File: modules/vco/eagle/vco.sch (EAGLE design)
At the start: 38 parts, among them IC1 TL074P, IC2 TL072P, Q1 J107, T1 2N3904, T2 2N3904

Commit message: Finish up 1x VCO schematic in eagle
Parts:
- added C10: 10p, rcl:C-EU025-024X044
- added C11, C12: 100p, rcl:C-EU025-024X044
- added C13, C14, C15, C16, C17, C18, C19, C20: 10u, rcl:CPOL-EUE1.8-4
- added C8: 2.2n, rcl:C-EU025-024X044
- added C9: 100n, rcl:C-EU025-024X044
- added D3, D4: 1N4148, diode:1N4148DO35-7
- added IC3, IC4: TL072P, linear:TL072P
- added R25: 2K, pot:TRIM_EU-B64Y
- added R26, R27, R28, R29, R41, R42, R54: 10K, resistor:R-EU_0204/7
- added R30, R31, R56: 100K, resistor:R-EU_0204/7
- added R32, R33: 1M, resistor:R-EU_0204/7
- added R34, R38: 15K, resistor:R-EU_0204/7
- added R35: 33K, resistor:R-EU_0204/7
- added R36, R58: 20K, resistor:R-EU_0204/7
- added R37, R50, R62: 1K, resistor:R-EU_0204/7
- added R39: 10K, pot:TRIM_EU-CA6V
- added R40: 390R, resistor:R-EU_0204/7
- added R43, R51, R52, R61: 22K, resistor:R-EU_0204/7
- added R44, R49: 4K7, resistor:R-EU_0204/7
- added R45, R46: 2K2, resistor:R-EU_0204/7
- added R47: 100K, pot:TRIM_EU-CA6V
- added R48: 50K, pot:TRIM_EU-CA6V
- added R53: 56K, resistor:R-EU_0204/7
- added R55: 150K, resistor:R-EU_0204/7
- added R57: 10M, resistor:R-EU_0204/7
- added R59: 8K2, resistor:R-EU_0204/7
- added R60: 3K3, resistor:R-EU_0204/7
- added T3, T4: 2N3904, transistor:2N3904
- added X1, X10, X2, X5, X6, X7, X8, X9: 22-23-2031, con-molex:22-23-2031
- added X11, X13, X3: (no value), con-wago-500:W237-103
- added X12, X4: (no value), con-wago-500:W237-102
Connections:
- new net N$19: R23.1, R25.E
- new net N$21: R24.2, R25.A
- new net N$24: IC3A.-IN, R34.2, R35.1
- new net N$25: IC2A.-IN, R25.S
- new net N$26: IC2B.+IN, R26.2, R27.1
- new net N$27: R28.1, X3-2.KL
- new net N$28: R5.1, X3-1.KL
- new net N$29: R29.1, X3-3.KL
- new net N$30: R29.2, X7-3.S
- new net N$31: R28.2, X5-3.S
- new net N$32: X5-2.S, X6-2.S
- new net N$33: X7-2.S, X8-2.S
- new net N$34: R30.1, X6-3.S
- new net N$35: R31.1, X8-3.S
- new net N$36: R32.1, X6-1.S
- new net N$37: R33.1, X8-1.S
- new net N$38: R52.1, X9-1.S
- new net N$39: C8.1, D3.C, D4.C, R34.1, R36.2
- new net N$40: R51.2, X9-3.S
- new net N$41: R54.1, X9-2.S
- new net N$42: D3.A, IC2B.OUT, R27.2, X12-1.KL
- new net N$43: R38.1, R39.A
- new net N$44: C9.1, IC3A.+IN, R39.S
- new net N$45: R40.2, R48.A, T3.E
- new net N$46: R40.1, R48.E, T4.E
- new net N$47: IC3B.-IN, R41.1, R44.2, T3.C
- new net N$48: IC3B.+IN, R42.1, R43.2, T4.C
- new net N$49: R53.1, X10-2.S, X10-3.S, X4-2.KL
- new net N$50: C10.2, IC4A.OUT, R57.2, R58.1
- new net N$51: IC3B.OUT, R44.1, R50.2
- new net N$52: R45.2, T4.B
- new net N$53: R46.2, R47.E, T3.B
- new net N$54: C11.1, C12.2, IC4B.-IN, R58.2, R59.1
- new net N$55: C11.2, IC4B.OUT, R59.2, R60.1
- new net N$56: R48.S, R49.2
- new net N$EXP-CV1: C1.2, IC1A.-IN, R1.2, R2.2, R3.1, R30.2, R31.2, R5.2
- new net N$LIN-CV1: C2.2, IC1B.-IN, R11.1, R32.2, R33.2, T1.C
- new net N$PULSE-OUT1: R60.2, R61.2, X11-1.KL
- new net N$PW-CV1: IC4A.+IN, R53.2, R54.2, R55.2
- new net N$SAW-OUT1: D4.A, IC2A.OUT, R21.2, R22.2, R26.1, R56.1, X12-2.KL
- new net N$SAW-OUT2: R62.2
- new net N$SINE-OUT1: R50.1, X11-2.KL
- new net N$TRI-OUT1: IC3A.OUT, R35.2, R37.2, R47.A, R47.S, X11-3.KL
- net GND: now also C12.1, C13.-, C14.+, C15.-, C16.+, C17.-, C18.+, C19.-, C20.+, C9.2, IC2B.-IN, IC4B.+IN, R22.1, R24.1, R37.1, R39.E, R43.1, R45.1, R46.1, R55.1, R61.1, R62.1, X10-1.S, X13-2.KL, X5-1.S, X7-1.S
- net N$1: now also R1.1, X1-2.S; no longer C1.2, IC1A.-IN, R1.2, R2.2, R3.1, R5.2
- net N$12: now also C10.1, IC4A.-IN, R56.2, R57.1; no longer C2.2, IC1B.-IN, R11.1, T1.C
- net N$14: now also R20.1
- net N$17: now also X4-1.KL
- net N$23: now also R2.1, X2-2.S; no longer IC2A.OUT, R21.2
- net VCC: now also C13.+, C15.+, C17.+, C19.+, IC1P.V+, IC2P.V+, IC3P.V+, IC4P.V+, R23.2, R38.2, R41.2, R42.2, R51.1, X1-3.S, X13-1.KL, X2-3.S
- net VEE: now also C14.-, C16.-, C18.-, C20.-, C8.2, IC1P.V-, IC2P.V-, IC3P.V-, IC4P.V-, R36.1, R49.1, R52.2, X1-1.S, X13-3.KL, X2-1.S
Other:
- note added: "100K LIN POT"
- note added: "FM1"
- note added: "FM1 DEPTH 100K LIN POT"
- note added: "FM1 EXP/LIN SPDT"
- note added: "FM2"
- note added: "FM2 DEPTH 100K LIN POT"
- note added: "FM2 EXP/LIN SPDT"
- note added: "POWER"
- note added: "PULSE OUT"
- note added: "PULSE WIDTH 100K LIN POT"
- note added: "PW"
- note added: "PWM DEPTH 100K LIN POT"
- note added: "RAMP OUT"
- note added: "SAW OUT"
- note added: "SINE OUT"
- note added: "TRIANGLE OUT"
- note removed: "TODO: - FM inputs - FM depth pot connectors - FM mode (EXP/LIN) switch connectors"
- moved on the sheet: C3, C4, C6, C7, D2, IC1C, IC1D, IC2A, IC2B, Q1, R12, R13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

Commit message: Add 2-layer VCO Eagle board design
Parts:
- added C21: 100n, rcl:C-EU025-024X044
- added IC5: TL072P, linear:TL072P
- added R63: 47R, resistor:R-EU_0204/7
- added R64: 1K, resistor:R-EU_0204/7
- added R65: 1M, resistor:R-EU_0204/7
- added X14, X15: 22-23-2031, con-molex:22-23-2031
- R4: value 3K3 -> 3K9
- R7: value 470R -> 390R
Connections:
- removed net N$42: D3.A, IC2B.OUT, R27.2, X12-1.KL
- new net N$57: R63.2, R8.E
- new net N$58: R64.1, X14-2.S, X14-3.S
- new net N$59: C21.1, IC5A.+IN, R64.2
- new net N$60: IC5A.-IN, IC5A.OUT, R6.1
- new net N$61: R65.1, X15-2.S
- net GND: now also C21.2, IC5B.+IN, IC5B.-IN
- net N$13: now also Q1.S; no longer Q1.D
- net N$14: now also Q1.D; no longer Q1.S
- net N$2: now also X14-1.S; no longer R6.1
- net N$4: now also R63.1; no longer R8.E
- net N$LIN-CV1: now also R65.2
- net N$SAW-OUT2: now also D3.A, IC2B.OUT, R27.2, X12-1.KL
- net VCC: now also IC5P.V+, X15-3.S
- net VEE: now also IC5P.V-, X15-1.S
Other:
- note added: "LIN DETUNE 100K LIN POT"
- note added: "PORTAMENTO 1M LIN POT"
- moved on the sheet: C10, C11, C12, C13, C14, C15, C16, C17, C18, C19, C20, C5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

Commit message: VCO PCB fixes
- Fixes a couple of design flaws: two opamps hade the inputs the wrong way
  around, the sine output net intersected with a pin connected to ground
- Moves the connector legend to the tName layer so they show up in fab.
- Adds legends to the trimpots
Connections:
- net GND: now also IC2B.+IN; no longer IC2B.-IN
- net N$22: now also IC2A.-IN; no longer IC2A.+IN
- net N$25: now also IC2A.+IN; no longer IC2A.-IN
- net N$26: now also IC2B.-IN; no longer IC2B.+IN
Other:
- moved on the sheet: IC2A, IC2B
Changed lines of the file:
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@@
 <instance part="SUPPLY11" gate="G$1" x="236.22" y="5.08" rot="R180"/>
 <instance part="R19" gate="G$1" x="165.1" y="-12.7" rot="R270"/>
-<instance part="IC2" gate="A" x="289.56" y="50.8"/>
-<instance part="IC2" gate="B" x="289.56" y="5.08"/>
+<instance part="IC2" gate="A" x="289.56" y="50.8" rot="MR180"/>
+<instance part="IC2" gate="B" x="289.56" y="5.08" rot="MR180"/>
 <instance part="R20" gate="G$1" x="271.78" y="53.34"/>
 <instance part="R21" gate="G$1" x="289.56" y="60.96"/>
@@
 </segment>
 <segment>
-<pinref part="IC2" gate="B" pin="-IN"/>
 <pinref part="SUPPLY15" gate="GND" pin="GND"/>
+<wire x1="279.4" y1="2.54" x2="279.4" y2="0" width="0.1524" layer="91"/>
+<pinref part="IC2" gate="B" pin="+IN"/>
 <wire x1="281.94" y1="2.54" x2="279.4" y2="2.54" width="0.1524" layer="91"/>
-<wire x1="279.4" y1="2.54" x2="279.4" y2="0" width="0.1524" layer="91"/>
 </segment>
 <segment>
@@
 <segment>
 <pinref part="R20" gate="G$1" pin="2"/>
-<pinref part="IC2" gate="A" pin="+IN"/>
 <wire x1="276.86" y1="53.34" x2="279.4" y2="53.34" width="0.1524" layer="91"/>
-<wire x1="281.94" y1="53.34" x2="279.4" y2="53.34" width="0.1524" layer="91"/>
 <wire x1="279.4" y1="53.34" x2="279.4" y2="60.96" width="0.1524" layer="91"/>
 <pinref part="R21" gate="G$1" pin="1"/>
 <wire x1="279.4" y1="60.96" x2="284.48" y2="60.96" width="0.1524" layer="91"/>
+<pinref part="IC2" gate="A" pin="-IN"/>
+<wire x1="279.4" y1="53.34" x2="281.94" y2="53.34" width="0.1524" layer="91"/>
 <junction x="279.4" y="53.34"/>
 </segment>
@@
 <pinref part="R25" gate="1" pin="S"/>
 <wire x1="269.24" y1="40.64" x2="269.24" y2="48.26" width="0.1524" layer="91"/>
-<pinref part="IC2" gate="A" pin="-IN"/>
-<wire x1="269.24" y1="48.26" x2="281.94" y2="48.26" width="0.1524" layer="91"/>
+<pinref part="IC2" gate="A" pin="+IN"/>
+<wire x1="281.94" y1="48.26" x2="269.24" y2="48.26" width="0.1524" layer="91"/>
 </segment>
 </net>
@@
 <segment>
 <pinref part="R26" gate="G$1" pin="2"/>
-<pinref part="IC2" gate="B" pin="+IN"/>
 <wire x1="276.86" y1="7.62" x2="279.4" y2="7.62" width="0.1524" layer="91"/>
 <pinref part="R27" gate="G$1" pin="1"/>
-<wire x1="279.4" y1="7.62" x2="281.94" y2="7.62" width="0.1524" layer="91"/>
 <wire x1="284.48" y1="15.24" x2="279.4" y2="15.24" width="0.1524" layer="91"/>
 <wire x1="279.4" y1="15.24" x2="279.4" y2="7.62" width="0.1524" layer="91"/>
+<pinref part="IC2" gate="B" pin="-IN"/>
+<wire x1="279.4" y1="7.62" x2="281.94" y2="7.62" width="0.1524" layer="91"/>
 <junction x="279.4" y="7.62"/>
 </segment>
@@
 <wire x1="294.64" y1="60.96" x2="299.72" y2="60.96" width="0.1524" layer="91"/>
 <wire x1="299.72" y1="60.96" x2="299.72" y2="50.8" width="0.1524" layer="91"/>
-<pinref part="IC2" gate="A" pin="OUT"/>
-<wire x1="299.72" y1="50.8" x2="297.18" y2="50.8" width="0.1524" layer="91"/>
 <junction x="299.72" y="50.8"/>
 <wire x1="299.72" y1="50.8" x2="307.34" y2="50.8" width="0.1524" layer="91"/>
@@
 <pinref part="X12" gate="-2" pin="KL"/>
 <wire x1="373.38" y1="-40.64" x2="375.92" y2="-40.64" width="0.1524" layer="91"/>
+<pinref part="IC2" gate="A" pin="OUT"/>
+<wire x1="297.18" y1="50.8" x2="299.72" y2="50.8" width="0.1524" layer="91"/>
 </segment>
 </net>
@@
 <wire x1="294.64" y1="15.24" x2="299.72" y2="15.24" width="0.1524" layer="91"/>
 <wire x1="299.72" y1="15.24" x2="299.72" y2="5.08" width="0.1524" layer="91"/>
-<pinref part="IC2" gate="B" pin="OUT"/>
-<wire x1="299.72" y1="5.08" x2="297.18" y2="5.08" width="0.1524" layer="91"/>
 <wire x1="299.72" y1="5.08" x2="307.34" y2="5.08" width="0.1524" layer="91"/>
 <wire x1="307.34" y1="5.08" x2="370.84" y2="5.08" width="0.1524" layer="91"/>
@@
 <junction x="299.72" y="5.08"/>
 <wire x1="307.34" y1="2.54" x2="307.34" y2="5.08" width="0.1524" layer="91"/>
-</segment>
-</net>
+<pinref part="IC2" gate="B" pin="OUT"/>
+<wire x1="297.18" y1="5.08" x2="299.72" y2="5.08" width="0.1524" layer="91"/>
+</segment>
+</net>

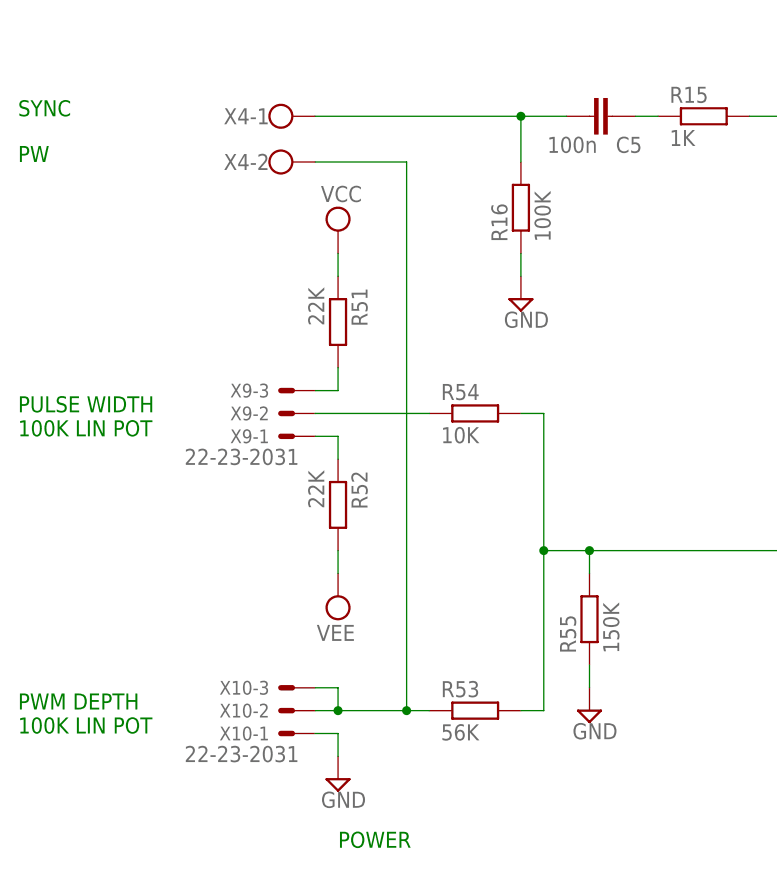
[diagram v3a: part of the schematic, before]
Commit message: Fix pwm amount input on VCO
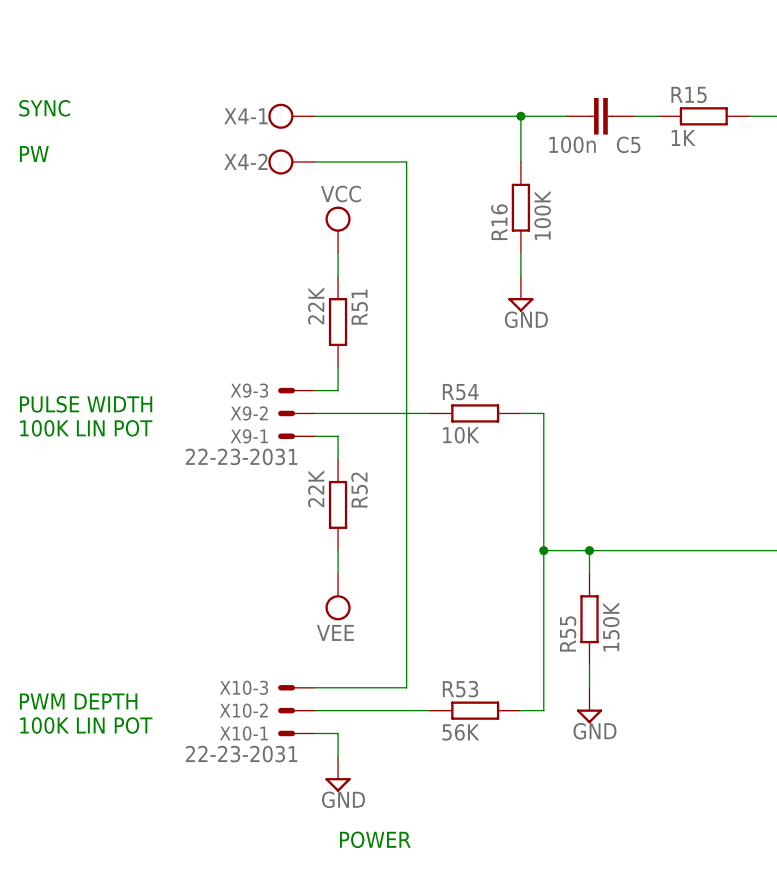
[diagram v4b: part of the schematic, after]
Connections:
- new net N$65: R53.1, X10-2.S
- net N$49: no longer R53.1, X10-2.S
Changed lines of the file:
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@@
 <net name="N$49" class="0">
 <segment>
-<pinref part="X10" gate="-2" pin="S"/>
-<wire x1="-12.7" y1="-132.08" x2="-10.16" y2="-132.08" width="0.1524" layer="91"/>
-<wire x1="-10.16" y1="-132.08" x2="-2.54" y2="-132.08" width="0.1524" layer="91"/>
-<wire x1="-2.54" y1="-132.08" x2="-2.54" y2="-71.12" width="0.1524" layer="91"/>
 <pinref part="X4" gate="-2" pin="KL"/>
+<wire x1="-2.54" y1="-129.54" x2="-2.54" y2="-71.12" width="0.1524" layer="91"/>
 <wire x1="-2.54" y1="-71.12" x2="-12.7" y2="-71.12" width="0.1524" layer="91"/>
-<pinref part="R53" gate="G$1" pin="1"/>
-<wire x1="0" y1="-132.08" x2="-2.54" y2="-132.08" width="0.1524" layer="91"/>
-<junction x="-2.54" y="-132.08"/>
 <pinref part="X10" gate="-3" pin="S"/>
-<wire x1="-12.7" y1="-129.54" x2="-10.16" y2="-129.54" width="0.1524" layer="91"/>
-<wire x1="-10.16" y1="-129.54" x2="-10.16" y2="-132.08" width="0.1524" layer="91"/>
-<junction x="-10.16" y="-132.08"/>
+<wire x1="-12.7" y1="-129.54" x2="-2.54" y2="-129.54" width="0.1524" layer="91"/>
 </segment>
 </net>
@@
 </segment>
 </net>
+<net name="N$65" class="0">
+<segment>
+<pinref part="X10" gate="-2" pin="S"/>
+<wire x1="-12.7" y1="-132.08" x2="0" y2="-132.08" width="0.1524" layer="91"/>
+<pinref part="R53" gate="G$1" pin="1"/>
+</segment>
+</net>
